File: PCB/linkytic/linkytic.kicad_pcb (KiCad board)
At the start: 2 copper layers, 65 x 43 mm, 10 parts, among them U1 AP7361C-33E, U1 M5333B, U2 cc2530

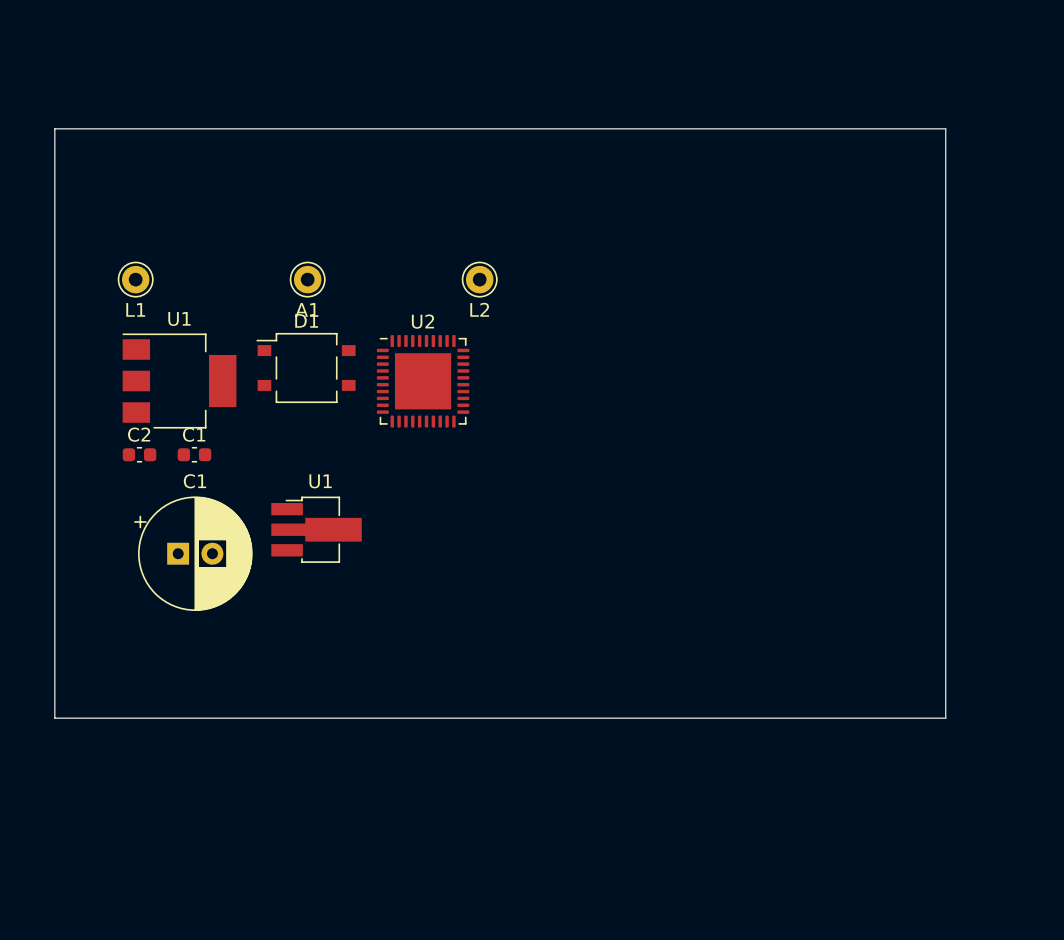
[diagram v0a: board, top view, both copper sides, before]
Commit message: Update with thermometre on same board
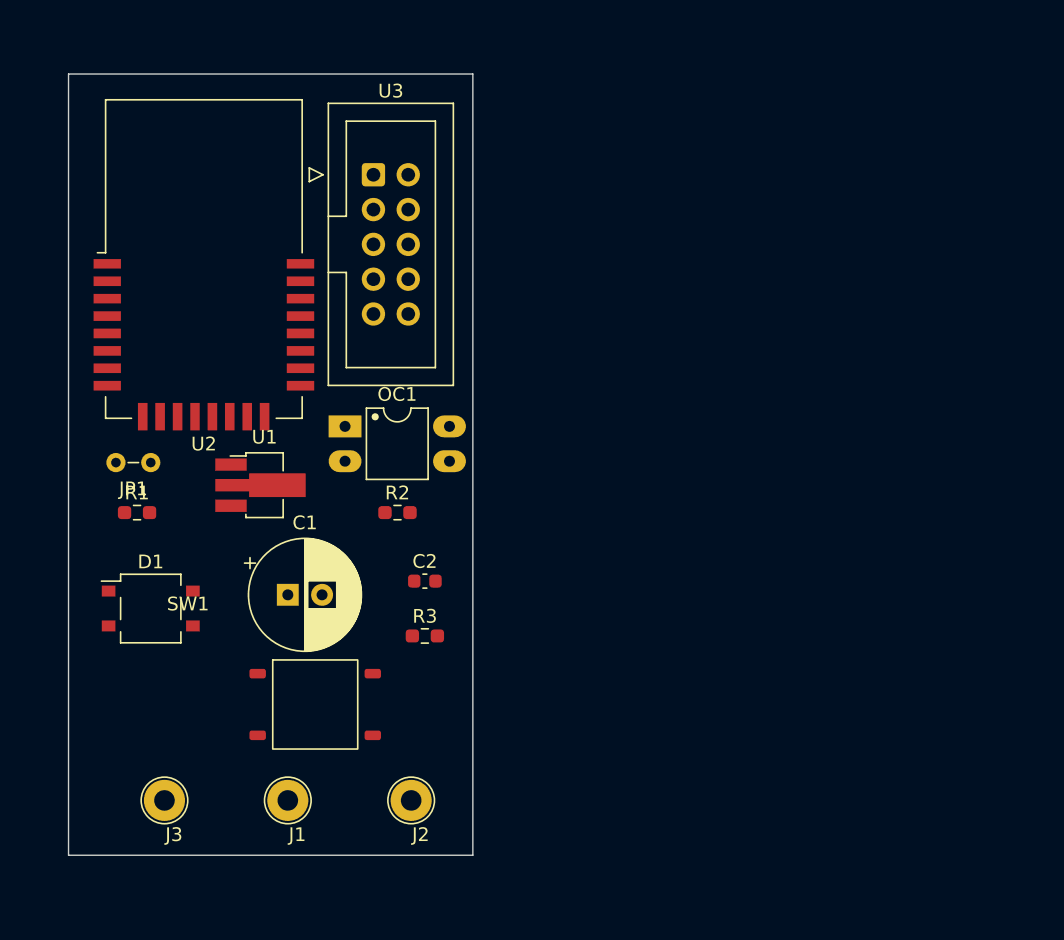
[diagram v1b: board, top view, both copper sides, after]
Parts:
- removed A1, L1, L2: Conn_01x01, Connector_Pin:Pin_D1.0mm_L10.0mm
- removed the C1 at (51.0, 73.0)
- removed the C1 at (52.2, 65.8)
- removed the U1 at (51.1, 60.4)
- removed the U1 at (61.1, 71.2)
- added C1: CP_Radial_D8.0mm_P2.50mm, Capacitor_THT_AKL:CP_Radial_D8.0mm_P2.50mm, F.Cu at (59.0, 76.0)
- added J1: L2, TestPoint:TestPoint_Loop_D2.54mm_Drill1.5mm_Beaded, F.Cu at (59.0, 91.0)
- added J2: L1, TestPoint:TestPoint_Loop_D2.54mm_Drill1.5mm_Beaded, F.Cu at (68.0, 91.0)
- added J3: A, TestPoint:TestPoint_Loop_D2.54mm_Drill1.5mm_Beaded, F.Cu at (50.0, 91.0)
- added JP1: Jumper_2_Open, Jumper_AKL:Jumper_P2.54mm_D0.7mm, F.Cu at (49.0, 66.3)
- added OC1: LTV-814, Package_DIP_AKL:DIP-4_W7.62mm_LongPads, F.Cu at (63.2, 63.7)
- added R1: 4.7k, Resistor_SMD:R_0603_1608Metric_Pad0.98x0.95mm_HandSolder, F.Cu at (48.0, 70.0)
- added R2: 10k, Resistor_SMD:R_0603_1608Metric_Pad0.98x0.95mm_HandSolder, F.Cu at (67.0, 70.0)
- added R3: 10k, Resistor_SMD:R_0603_1608Metric_Pad0.98x0.95mm_HandSolder, F.Cu at (69.0, 79.0)
- added SW1: SW_Push_Open, Library:interrupteur, F.Cu at (56.8, 81.8)
- added U1: M5333B, Package_TO_SOT_SMD:SOT-89-3_Handsoldering, F.Cu at (57.0, 68.0)
- added U3: CC_debugger, Connector_IDC:IDC-Header_2x05_P2.54mm_Vertical, F.Cu at (65.2, 45.4)
- U2: value cc2530 -> E18-MS1-PCB; footprint Package_DFN_QFN:HVQFN-40-1EP_6x6mm_P0.5mm_EP4.1x4.1mm -> RF_Module:E18-MS1-PCB
- moved C2 22.8 mm to (69.0, 75.0)
- moved D1 20.9 mm to (49.0, 77.0)
- moved U2 18.3 mm to (52.9, 51.5)
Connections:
- U2 pad 1: unconnected-(U2-Pad1) -> GND
- U2 pad 16: unconnected-(U2-Pad16) -> Net-(R3-Pad1)
- U2 pad 2: unconnected-(U2-Pad2) -> Net-(JP1-Pad2)
- U2 pad 21: unconnected-(U2-Pad21) -> Net-(OC1-Pad4)
- U2 pad 24: unconnected-(U2-Pad24) -> Net-(U2-Pad24)
- U2 pad 3: unconnected-(U2-Pad3) -> Net-(U2-Pad3)
- U2 pad 4: unconnected-(U2-Pad4) -> Net-(U2-Pad4)
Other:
- board size 65 x 43 mm -> 29.5 x 57 mm

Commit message: first version, that will notwork :/
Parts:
- removed JP1: Jumper_2_Open, Jumper_AKL:Jumper_P2.54mm_D0.7mm
- SW1: value SW_Push_Open -> benoit
- moved R3 22.4 mm to (49.0, 69.0), turned to 180 degrees
- moved OC1 20.0 mm to (51.2, 79.7)
- moved J2 19.5 mm to (48.6, 89.0)
- moved SW1 15.2 mm to (62.8, 67.8)
- moved C2 14.4 mm to (57.0, 67.0)
- moved J3 14.3 mm to (64.2, 89.0)
- moved R1 10.2 mm to (46.1, 80.0)
- moved C1 8.06 mm to (66.0, 80.0)
- moved R2 5.12 mm to (65.9, 65.0)
- moved U1 4.12 mm to (58.0, 72.0)
- moved J1 3.16 mm to (56.4, 89.2)
- moved D1 2.00 mm to (49.0, 75.0)
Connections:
- R3 pad 2: Net-(JP1-Pad2) -> 3v3
- U2 pad 2: Net-(JP1-Pad2) -> 3v3
- U3 pad 9: Net-(JP1-Pad2) -> 3v3
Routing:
- net 3v3: track 0.00 -> 58.0 mm, vias 0 -> 4
- net Net-(OC1-Pad4): track 0.00 -> 30.9 mm, vias 0 -> 2
- net Net-(R3-Pad1): track 0.00 -> 30.5 mm, vias 0 -> 2
- net Net-(U2-Pad4): track 0.00 -> 25.2 mm
- net Net-(D1-Pad2): track 0.00 -> 23.5 mm
- net Net-(U2-Pad3): track 0.00 -> 22.1 mm
- net Net-(C1-Pad1): track 0.00 -> 21.0 mm
- net GND: track 0.00 -> 18.0 mm, vias 0 -> 4
- net Net-(D1-Pad1): track 0.00 -> 17.1 mm
- net Net-(J1-Pad1): track 0.00 -> 9.10 mm
- net Net-(U2-Pad24): track 0.00 -> 5.79 mm
- net Net-(OC1-Pad1): track 0.00 -> 4.29 mm
- added copper zone on B.Cu, net GND

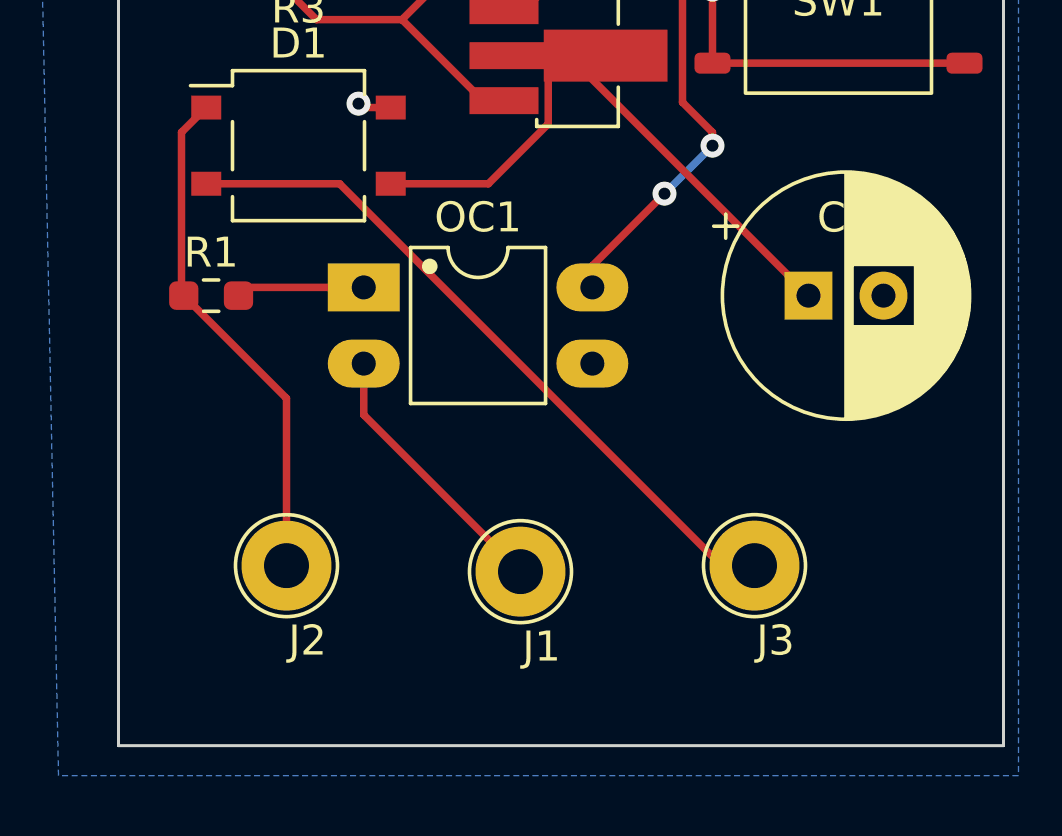
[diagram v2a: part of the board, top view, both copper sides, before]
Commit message: update with A/L1 reversedé
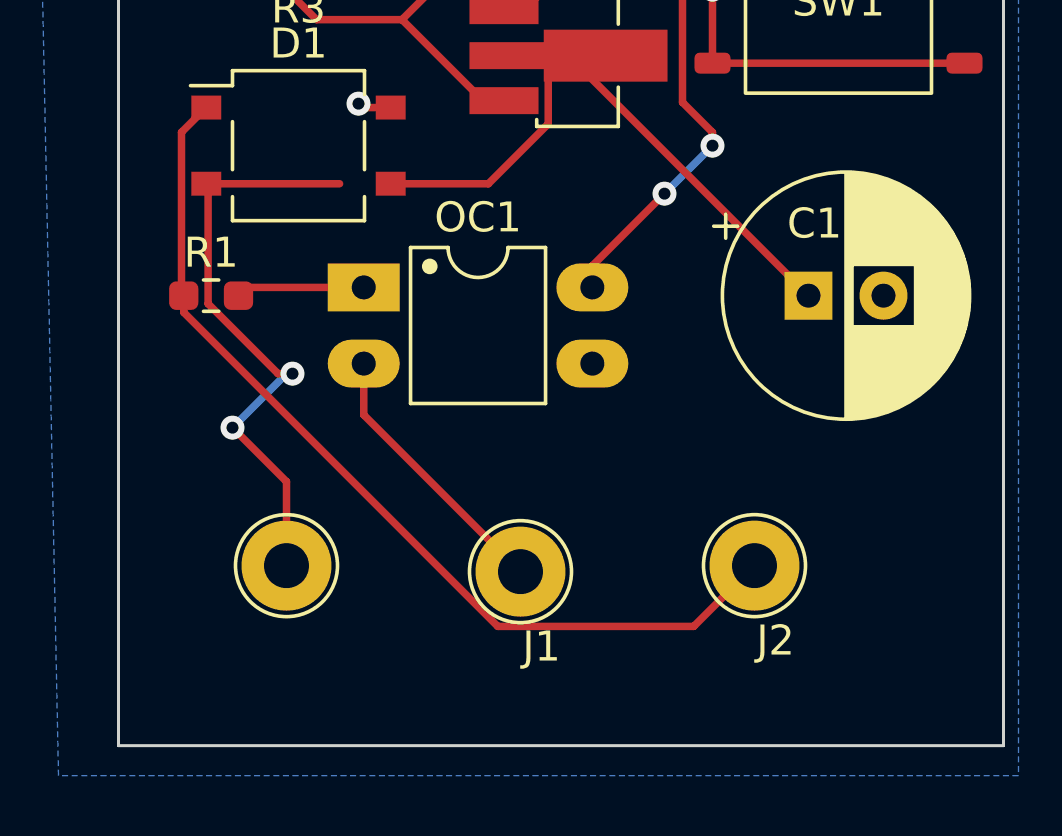
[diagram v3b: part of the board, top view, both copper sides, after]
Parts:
- moved J2 15.6 mm to (64.2, 89.0)
- moved J3 15.6 mm to (48.6, 89.0)
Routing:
- net Net-(D1-Pad1): track 17.1 -> 32.5 mm
- net Net-(D1-Pad2): track 23.5 -> 20.3 mm, vias 0 -> 2
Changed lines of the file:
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@@
   (net 29 "Net-(J1-Pad1)")
   (footprint "TestPoint:TestPoint_Loop_D2.54mm_Drill1.5mm_Beaded" (layer "F.Cu")
-    (at 64.2 89)
+    (at 48.6 89)
     (descr "wire loop with bead as test point, loop diameter2.548mm, hole diameter 1.5mm")
     (tags "test point wire loop bead")
@@
     (property "Sheetname" "")
     (attr through_hole)
-    (fp_text reference "J3" (at 0.7 2.5) (layer "F.SilkS")
-      (effects (font (size 1 1) (thickness 0.15)))
-    )
-    (fp_text value "A" (at 0 -2.8) (layer "F.Fab")
+    (fp_text reference "J3" (at 0.7 2.5) (layer "B.SilkS")
+      (effects (font (size 1 1) (thickness 0.15)))
+    )
+    (fp_text value "A" (at 0 -2.8) (layer "B.SilkS")
       (effects (font (size 1 1) (thickness 0.15)))
     )
@@
     (property "Sheetname" "")
     (attr through_hole)
-    (fp_text reference "C1" (at 1.2 -2.6) (layer "F.SilkS")
+    (fp_text reference "C1" (at 0.2 -2.4) (layer "F.SilkS")
       (effects (font (size 1 1) (thickness 0.15)))
     )
@@
   )
   (footprint "TestPoint:TestPoint_Loop_D2.54mm_Drill1.5mm_Beaded" (layer "F.Cu")
-    (at 48.6 89)
+    (at 64.2 89)
     (descr "wire loop with bead as test point, loop diameter2.548mm, hole diameter 1.5mm")
     (tags "test point wire loop bead")
@@
       (effects (font (size 1 1) (thickness 0.15)))
     )
-    (fp_text value "L1" (at 0 -2.8) (layer "F.Fab")
+    (fp_text value "L1" (at 0 -2.8) (layer "B.SilkS")
       (effects (font (size 1 1) (thickness 0.15)))
     )
@@
       (effects (font (size 1 1) (thickness 0.15)))
     )
-    (fp_text value "L2" (at 0 -2.8) (layer "F.Fab")
+    (fp_text value "L2" (at 0 -2.8) (layer "B.SilkS")
       (effects (font (size 1 1) (thickness 0.15)))
     )
@@
   )
   (gr_rect (start 43 38) (end 72.5 95) (layer "Edge.Cuts") (width 0.1) (fill none))
-  (segment (start 63.1 89) (end 50.37 76.27) (width 0.25) (layer "F.Cu") (net 1))
-  (segment (start 64.2 89) (end 63.1 89) (width 0.25) (layer "F.Cu") (net 1))
+  (segment (start 48.6 86.2) (end 46.8 84.4) (width 0.25) (layer "F.Cu") (net 1))
+  (segment (start 48.8 82.6) (end 48.317005 82.6) (width 0.25) (layer "F.Cu") (net 1))
+  (segment (start 45.9875 76.3325) (end 45.925 76.27) (width 0.25) (layer "F.Cu") (net 1))
+  (segment (start 48.6 89) (end 48.6 86.2) (width 0.25) (layer "F.Cu") (net 1))
+  (segment (start 45.9875 80.270495) (end 45.9875 76.3325) (width 0.25) (layer "F.Cu") (net 1))
   (segment (start 50.37 76.27) (end 45.925 76.27) (width 0.25) (layer "F.Cu") (net 1))
+  (segment (start 48.317005 82.6) (end 45.9875 80.270495) (width 0.25) (layer "F.Cu") (net 1))
+  (via (at 48.8 82.6) (size 0.8) (drill 0.4) (layers "F.Cu" "B.Cu") (net 1))
+  (via (at 46.8 84.4) (size 0.8) (drill 0.4) (layers "F.Cu" "B.Cu") (net 1))
+  (segment (start 46.8 84.4) (end 48.6 82.6) (width 0.25) (layer "B.Cu") (net 1))
+  (segment (start 48.6 82.6) (end 48.8 82.6) (width 0.25) (layer "B.Cu") (net 1))
   (segment (start 55.33 76.27) (end 57.325 74.275) (width 0.25) (layer "F.Cu") (net 2))
   (segment (start 58 72) (end 55.9375 72) (width 0.25) (layer "F.Cu") (net 2))
@@
   (segment (start 45.1 74.555) (end 45.1 79.925) (width 0.25) (layer "F.Cu") (net 5))
   (segment (start 45.1 79.925) (end 45.175 80) (width 0.25) (layer "F.Cu") (net 5))
+  (segment (start 64.2 89) (end 63.1 89) (width 0.25) (layer "F.Cu") (net 5))
+  (segment (start 55.64406 91.025) (end 62.175 91.025) (width 0.25) (layer "F.Cu") (net 5))
+  (segment (start 45.175 80.55594) (end 55.64406 91.025) (width 0.25) (layer "F.Cu") (net 5))
+  (segment (start 45.175 80) (end 45.175 80.55594) (width 0.25) (layer "F.Cu") (net 5))
+  (segment (start 62.175 91.025) (end 64.2 89) (width 0.25) (layer "F.Cu") (net 5))
   (segment (start 45.925 73.73) (end 45.1 74.555) (width 0.25) (layer "F.Cu") (net 5))
-  (segment (start 48.6 89) (end 48.6 83.425) (width 0.25) (layer "F.Cu") (net 5))
-  (segment (start 48.6 83.425) (end 45.175 80) (width 0.25) (layer "F.Cu") (net 5))
   (segment (start 47.275 79.725) (end 51.175 79.725) (width 0.25) (layer "F.Cu") (net 23))
   (segment (start 47 80) (end 47.275 79.725) (width 0.25) (layer "F.Cu") (net 23))

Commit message: save before usb adding, last modif
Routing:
- net Net-(D1-Pad2): track 20.3 -> 15.9 mm
- net Net-(D1-Pad1): track 32.5 -> 31.4 mm
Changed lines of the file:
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@@
   (segment (start 48.6 89) (end 48.6 86.2) (width 0.25) (layer "F.Cu") (net 1))
   (segment (start 45.9875 80.270495) (end 45.9875 76.3325) (width 0.25) (layer "F.Cu") (net 1))
-  (segment (start 50.37 76.27) (end 45.925 76.27) (width 0.25) (layer "F.Cu") (net 1))
   (segment (start 48.317005 82.6) (end 45.9875 80.270495) (width 0.25) (layer "F.Cu") (net 1))
   (via (at 48.8 82.6) (size 0.8) (drill 0.4) (layers "F.Cu" "B.Cu") (net 1))
@@
   (segment (start 45.1 74.555) (end 45.1 79.925) (width 0.25) (layer "F.Cu") (net 5))
   (segment (start 45.1 79.925) (end 45.175 80) (width 0.25) (layer "F.Cu") (net 5))
-  (segment (start 64.2 89) (end 63.1 89) (width 0.25) (layer "F.Cu") (net 5))
   (segment (start 55.64406 91.025) (end 62.175 91.025) (width 0.25) (layer "F.Cu") (net 5))
   (segment (start 45.175 80.55594) (end 55.64406 91.025) (width 0.25) (layer "F.Cu") (net 5))

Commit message: Update final version V0
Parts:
- added -: BAT-, Connector_PinHeader_1.27mm:PinHeader_1x01_P1.27mm_Vertical, F.Cu at (88.8, 78.4)
- added C3: 1u, Capacitor_SMD:C_0603_1608Metric, B.Cu at (88.6, 72.8)
- added C4: 10uF, Capacitor_SMD:C_0603_1608Metric, F.Cu at (92.0, 70.4)
- added D2: GREENLED, LED_SMD:LED_0805_2012Metric_Pad1.15x1.40mm_HandSolder, B.Cu at (90.4, 86.2)
- added D3: REDLED, LED_SMD:LED_0805_2012Metric_Pad1.15x1.40mm_HandSolder, B.Cu at (90.4, 83.4)
- added D4: SS24, Diode_SMD_AKL:D_SMB, B.Cu at (86.2, 51.4)
- added J5: BAT+, Connector_PinHeader_1.27mm:PinHeader_1x01_P1.27mm_Vertical, F.Cu at (92.6, 78.4)
- added J6: USB_B_Micro, usb:USB_aliexpress, B.Cu at (79.4, 87.2)
- added Q1: AO3407A, Package_TO_SOT_SMD_AKL:SOT-23, F.Cu at (88.0, 67.4)
- added R4: 100k, Resistor_SMD:R_0603_1608Metric_Pad0.98x0.95mm_HandSolder, F.Cu at (87.5, 75.8)
- added R5: 1k, Resistor_SMD:R_0603_1608Metric_Pad0.98x0.95mm_HandSolder, F.Cu at (87.7, 73.4)
- added R6: 10k, Resistor_SMD:R_0603_1608Metric_Pad0.98x0.95mm_HandSolder, F.Cu at (88.1, 70.6)
- added R7: 1k, Resistor_SMD:R_0603_1608Metric_Pad0.98x0.95mm_HandSolder, F.Cu at (92.1, 67.0)
- added R8: 1.2k, Resistor_SMD:R_0603_1608Metric_Pad0.98x0.95mm_HandSolder, B.Cu at (87.3, 60.6)
- added R9: 10k, Resistor_SMD:R_0603_1608Metric_Pad0.98x0.95mm_HandSolder, F.Cu at (91.9, 73.6)
- added SW2: benoit2, Library:interrupteur, B.Cu at (83.4, 55.0)
- added U4: TP4056, Package_SO:SOP-8_3.76x4.96mm_P1.27mm, F.Cu at (80.3, 67.2)
- added U5: M5333B, Package_TO_SOT_SMD:SOT-89-3_Handsoldering, B.Cu at (86.6, 57.2)
- added U6: CC_debugger, Connector_IDC:IDC-Header_2x05_P2.54mm_Vertical, B.Cu at (83.0, 71.3)
- added U7: E18-MS1-PCB, RF_Module:E18-MS1-PCB, F.Cu at (84.8, 50.7)
- added U8: DS18B20, Package_TO_SOT_THT:TO-92_Inline, B.Cu at (91.4, 91.4)
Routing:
- net GND_2: track 0.00 -> 91.3 mm, vias 0 -> 11
- net USB_IN: track 0.00 -> 65.3 mm, vias 0 -> 2
- net VDD2: track 0.00 -> 63.1 mm, vias 0 -> 4
- net Net-(R6-Pad1): track 0.00 -> 53.6 mm, vias 0 -> 1
- net Net-(U6-Pad7): track 0.00 -> 42.9 mm
- net Net-(D4-Pad1): track 0.00 -> 32.3 mm, vias 0 -> 3
- net Net-(U6-Pad3): track 0.00 -> 29.1 mm, vias 0 -> 1
- net Net-(U6-Pad4): track 0.00 -> 25.6 mm
- net Net-(J5-Pad1): track 0.00 -> 21.1 mm, vias 0 -> 3
- net Net-(R9-Pad1): track 0.00 -> 21.0 mm, vias 0 -> 2
- net Net-(D3-Pad1): track 0.00 -> 19.0 mm, vias 0 -> 1
- net Net-(D2-Pad1): track 0.00 -> 18.4 mm, vias 0 -> 3
- net Net-(R8-Pad2): track 0.00 -> 13.8 mm, vias 0 -> 3
- net Net-(R7-Pad2): track 0.00 -> 11.7 mm, vias 0 -> 2
- net Net-(R5-Pad2): track 0.00 -> 9.40 mm
- added copper zone on B.Cu, net GND_2
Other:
- board size 29.5 x 57 mm -> 51.9 x 57 mm
- board text added: "LINKYTIC MBE V0"
- board text added: "Zigbee Thermometer V0 MBE"
